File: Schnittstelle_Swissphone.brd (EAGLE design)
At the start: 82 x 64 mm, 22 parts, among them IC1 FT232RL, IC2 LM317LD

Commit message: add Arduino Nano and ENC28J60
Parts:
- removed U$3: WEMOS-D1-MINI-PRO, diy-modules:WEMOS-D1-MINI-PRO
- added M1: ARDUINO-NANO-3.0, diy-modules:ARDUINO-NANO-3.0
- added M2: ETHERNET-ENC28J60, diy-modules:ETHERNET-ENC28J60
- moved SV4 143.8 mm to (-53.7, -70.9), turned to 0 degrees
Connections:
- removed net 3V3: U$3.JP1.8
- new net +3V3: M1.J2.14, M2.2
- new net +5V: C4.1, IC2.1, L1.1, M1.J2.4, M2.12, POWER.A, SV3.5, SV4.6, U$1.P$7
- new net N$18: M1.J1.8, SV4.5
- new net N$19: M1.J1.9, SV4.3
- new net N$20: M1.J1.10, SV4.1
- new net N$21: M1.J1.11, SV4.4
- new net VIN: M1.J2.1
- net GND: now also M1.J1.4, M1.J2.2, M2.1, M2.11, SV4.2; no longer SV4.6, U$3.JP2.7
- net N$11: now also M1.J1.15, M2.8; no longer C4.1, IC2.1, L1.1, POWER.A, SV3.5, SV4.2, U$1.P$7, U$3.JP2.8
- net N$15: now also M1.J2.15, M2.6; no longer SV4.3, U$3.JP1.4
- net N$16: now also M1.J1.14, M2.5; no longer SV4.5, U$3.JP1.3
- net N$17: now also M1.J1.13, M2.3; no longer SV4.4, U$3.JP1.1
- net N$5: no longer U$3.JP2.2
- net N$6: no longer U$3.JP2.1
- net N$8: now also M1.J1.5, M2.10; no longer SV4.1, U$3.JP1.5

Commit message: Add Layout
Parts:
- added SJ1, SJ2: (no value), jumper:SJ
- moved M2 132.7 mm to (62.4, 44.8), turned to 180 degrees
- moved M1 107.8 mm to (64.7, 17.4), turned to 180 degrees
- moved SV4 106.4 mm to (6.20, 17.0), turned to 270 degrees
- moved U$2 86.7 mm to (11.4, 1.83)
- moved U$1 61.7 mm to (17.0, 66.5), turned to 180 degrees
- moved SV2 52.5 mm to (30.6, 65.2), turned to 180 degrees
- moved RX 44.3 mm to (14.7, 56.3), turned to 180 degrees
- moved R2 43.9 mm to (19.6, 53.6)
- moved R1 35.3 mm to (19.6, 49.2)
- moved R3 34.3 mm to (29.1, 46.3), turned to 90 degrees
- moved IC2 33.4 mm to (28.5, 54.5)
- moved L1 33.4 mm to (15.9, 25.0), turned to 90 degrees
- moved TX 30.3 mm to (14.6, 49.8), turned to 180 degrees
- moved C4 29.8 mm to (26.6, 48.2)
- moved C3 29.6 mm to (22.0, 34.9), turned to 90 degrees
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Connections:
- removed net N$5: IC1.1, SV1.6
- new net N$22: M1.J1.2, SJ1.1
- new net N$23: IC1.22, R2.1
- new net N$24: IC1.1, SJ1.2, SV1.6
- net N$2: now also R2.2, RX.K; no longer IC1.22, R2.1
- net N$4: now also M1.J1.1, SJ2.1; no longer R2.2, RX.K
- net N$6: now also SJ2.2
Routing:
- net +5V: track 0.00 -> 164.9 mm
- net N$20: track 0.00 -> 80.5 mm
- net VCC: track 0.00 -> 80.3 mm
- net N$17: track 0.00 -> 77.0 mm
- net N$18: track 0.00 -> 71.1 mm
- net N$21: track 0.00 -> 68.0 mm
- net N$19: track 0.00 -> 67.5 mm
- net N$11: track 0.00 -> 64.0 mm
- net N$16: track 0.00 -> 60.7 mm
- net +3V3: track 0.00 -> 54.9 mm
- net N$15: track 0.00 -> 54.2 mm, vias 0 -> 1
- net N$7: track 0.00 -> 48.9 mm, vias 0 -> 2
- net N$24: track 0.00 -> 38.7 mm, vias 0 -> 2
- net N$6: track 0.00 -> 38.5 mm, vias 0 -> 1
- net N$8: track 0.00 -> 37.4 mm
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- added copper zone on layer 1, net GND
- added copper zone on layer 16, net GND
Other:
- board size 82 x 64 mm -> 88 x 70 mm

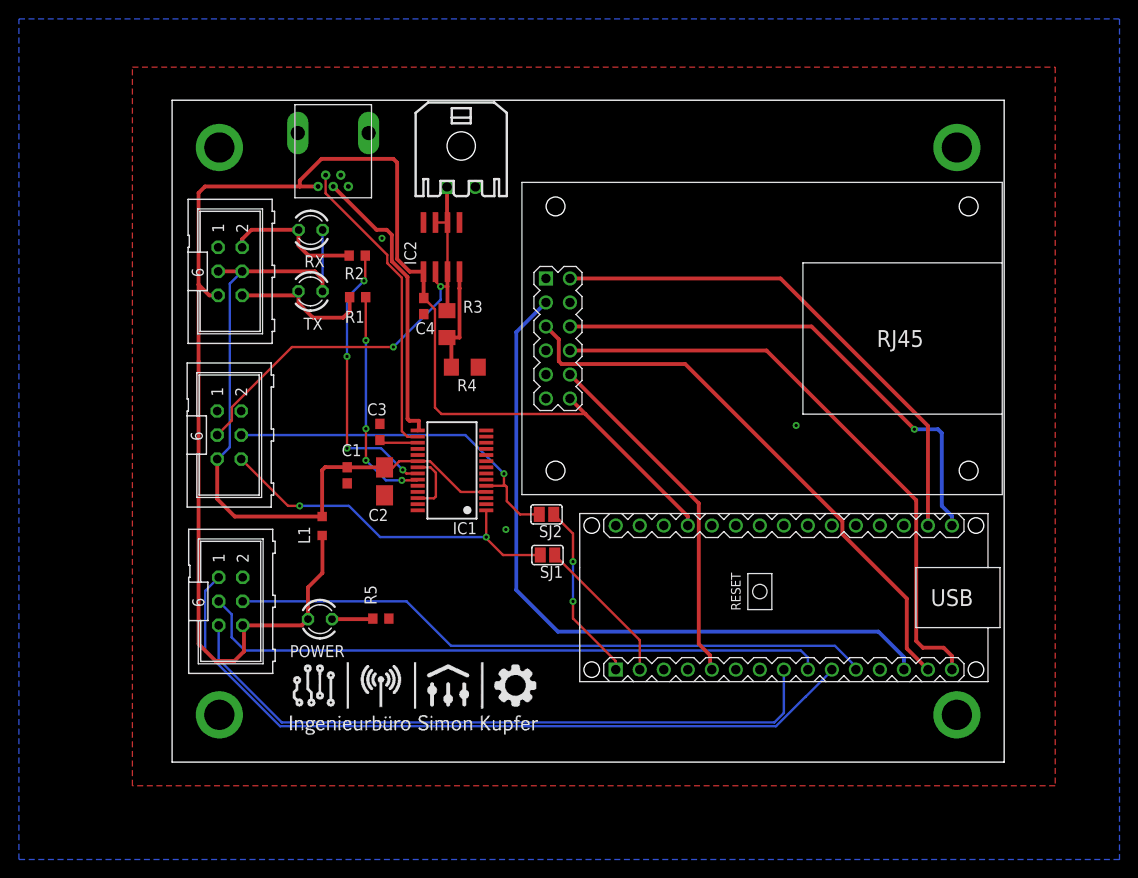
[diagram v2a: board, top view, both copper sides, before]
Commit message: PCB wo. Ethernet
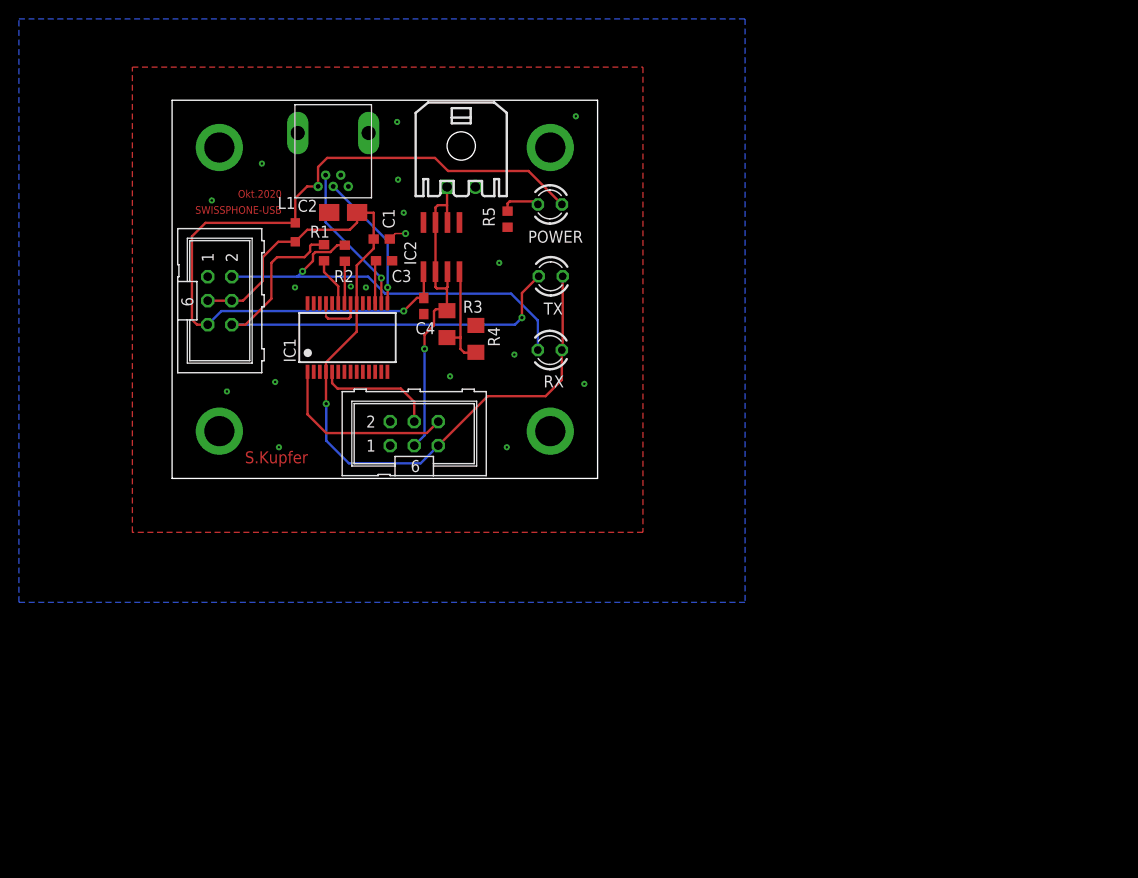
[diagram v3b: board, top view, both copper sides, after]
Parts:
- removed M1: ARDUINO-NANO-3.0, diy-modules:ARDUINO-NANO-3.0
- removed M2: ETHERNET-ENC28J60, diy-modules:ETHERNET-ENC28J60
- removed SJ1, SJ2: (no value), jumper:SJ
- removed SV4: (no value), con-harting-ml:ML6
- removed U$2: SK, EigeneLogos:INGSK
- moved POWER 50.2 mm to (40.0, 59.0), turned to 180 degrees
- moved R5 44.3 mm to (35.5, 57.4), turned to 90 degrees
- moved L1 31.2 mm to (13.0, 56.0), turned to 270 degrees
- moved C2 28.8 mm to (18.1, 58.1), turned to 0 degrees
- moved RX 28.3 mm to (40.0, 43.6)
- moved TX 25.5 mm to (40.0, 51.4)
- moved C1 25.3 mm to (22.2, 55.3), turned to 0 degrees
- moved SV1 19.6 mm to (25.6, 34.7), turned to 0 degrees
- moved C3 18.1 mm to (22.4, 53.0), turned to 0 degrees
- moved IC1 17.9 mm to (18.6, 44.9), turned to 0 degrees
- moved R1 5.90 mm to (16.1, 53.9), turned to 90 degrees
- moved SV3 3.29 mm to (5.04, 48.8)
- moved R4 3.21 mm to (32.1, 44.8), turned to 270 degrees
- moved R2 1.33 mm to (18.3, 53.8), turned to 90 degrees
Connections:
- removed net +3V3: M1.J2.14, M2.2
- removed net N$11: M1.J1.15, M2.8
- removed net N$15: M1.J2.15, M2.6
- removed net N$16: M1.J1.14, M2.5
- removed net N$17: M1.J1.13, M2.3
- removed net N$18: M1.J1.8, SV4.5
- removed net N$19: M1.J1.9, SV4.3
- removed net N$20: M1.J1.10, SV4.1
- removed net N$21: M1.J1.11, SV4.4
- removed net N$22: M1.J1.2, SJ1.1
- removed net N$4: M1.J1.1, SJ2.1
- removed net N$8: M1.J1.5, M2.10
- removed net VIN: M1.J2.1
- net +5V: no longer M1.J2.4, M2.12, SV4.6
- net GND: no longer M1.J1.4, M1.J2.2, M2.1, M2.11, SV4.2
- net N$24: no longer SJ1.2
- net N$6: no longer SJ2.2
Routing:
- net N$20: track 80.5 -> 0.00 mm
- net +5V: track 164.9 -> 84.9 mm, vias 0 -> 1
- net N$17: track 77.0 -> 0.00 mm
- net N$18: track 71.1 -> 0.00 mm
- net N$21: track 68.0 -> 0.00 mm
- net N$19: track 67.5 -> 0.00 mm
- net N$11: track 64.0 -> 0.00 mm
- net N$16: track 60.7 -> 0.00 mm
- net +3V3: track 54.9 -> 0.00 mm
- net N$15: track 54.2 -> 0.00 mm, vias 1 -> 0
- net N$8: track 37.4 -> 0.00 mm
- net N$3: track 15.2 -> 52.0 mm, vias 0 -> 1
- net N$2: track 14.7 -> 44.2 mm, vias 0 -> 1
- net N$6: track 38.5 -> 12.8 mm, vias 1 -> 0
- net N$23: track 29.8 -> 4.46 mm, vias 4 -> 0
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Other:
- board size 88 x 70 mm -> 45 x 40 mm
- board text added: "Okt.2020"
- board text added: "S.Kupfer"
- board text added: "SWISSPHONE-USB"

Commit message: -
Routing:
- net GND: vias 22 -> 23
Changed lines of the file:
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@@
 <wire x1="23.02" y1="55.32" x2="23.6" y2="55.9" width="0.1524" layer="1"/>
 <wire x1="23.6" y1="55.9" x2="24.7" y2="55.9" width="0.1524" layer="1"/>
+<via x="11.4" y="54.2" extent="1-16" drill="0.25"/>
 </signal>
 <signal name="N$7">

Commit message: bug fixes
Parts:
- removed U$1: MINI USB, simon:USBBWM
- added U$2: MINI USB, simon:USBBWM
- moved POWER 1.48 mm to (40.0, 57.5)
- moved TX 1.38 mm to (40.0, 50.0)
- moved R5 1.17 mm to (34.6, 56.6), turned to 0 degrees
- moved RX 1.08 mm to (40.0, 42.5)
- moved C3 0.10 mm to (22.3, 53.0)
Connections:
- net +5V: now also U$2.P$3; no longer SV3.5, U$1.P$7
- net GND: now also U$2.P$1, U$2.P$2, U$2.P$7; no longer U$1.P$1, U$1.P$2, U$1.P$3
- net N$12: now also SV3.5
- net N$13: now also U$2.P$4; no longer U$1.P$6
- net N$14: now also U$2.P$5; no longer U$1.P$5
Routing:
- net N$12: track 4.24 -> 47.6 mm, vias 0 -> 1
- net +5V: track 84.9 -> 56.4 mm, vias 1 -> 0
- net GND: track 7.54 -> 5.62 mm, vias 23 -> 22
- net N$3: track 52.0 -> 50.6 mm
- net N$2: track 44.2 -> 45.3 mm
- net N$13: track 16.0 -> 17.0 mm, vias 1 -> 0
- net VCC: track 90.5 -> 89.7 mm
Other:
- board text added: "DME-USB"
- board text removed: "SWISSPHONE-USB"
